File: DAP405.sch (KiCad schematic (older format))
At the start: 56 parts, among them J1 USB_B, J2 Target, J3 JTAG, U1 LT1117-3.3, U10 74LVC1G17, U11 SN74LVC1T45DBV, U12 SN74LVC1T45DBV, U13 SN74LVC1T45DBV, U14 SY6280, U2 USB3300-EZK, U3 STM32F405RGTx, U4 REF3033, U5 74LVC1G17, U6 SN74LVC1T45DBV, U7 SN74LVC1T45DBV, U8 SN74LVC1T45DBV, U9 SN74LVC1T45DBV, Y1 24M, Y2 12M

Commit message: Fixing the ULPI interface.
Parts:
- added D4: SMF5.0A, Diode_SMD:D_1206_3216Metric_Pad1.42x1.75mm_HandSolder, symbol Device:D_Zener_Small
- added F2: 200mA, Fuse:Fuse_0805_2012Metric_Pad1.15x1.40mm_HandSolder, symbol Device:Polyfuse_Small
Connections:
- net GND: now also D4.2 (A)
- net VDD: now also D4.1 (K), F2.2; no longer J2.1 (Pin_1)
- net ~RESET: no longer U2.9 (RESET)
- net ULPI_RST: now reaches U3.37 (PC6)
- net ULPI_RST: now also U2.9 (RESET)
- new net: F2.1, J2.1 (Pin_1)
- no-connect marks 22 -> 21
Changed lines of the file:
@@
 EESchema Schematic File Version 4
+LIBS:DAP405-cache
 EELAYER 29 0
 EELAYER END
@@
 ULPI_CLK
 Text Label 4000 4400 2    50   ~ 0
-~RESET
+ULPI_RST
 Wire Wire Line
 	4000 3200 3400 3200
@@
 Wire Wire Line
 	5400 6500 5400 6600
-Wire Wire Line
-	4750 6300 4100 6300
-Wire Wire Line
-	4100 6300 4100 6200
 NoConn ~ 5250 6300
 Text Label 4400 6400 0    50   ~ 0
@@
 Wire Wire Line
 	4100 6800 4750 6800
-Wire Wire Line
-	4100 6300 4100 6500
-Connection ~ 4100 6300
 Wire Wire Line
 	4100 6800 4100 6700
@@
 NoConn ~ 6900 2600
 NoConn ~ 5500 3600
-NoConn ~ 5500 3700
 NoConn ~ 5500 4100
+Text Label 5100 3700 0    50   ~ 0
+ULPI_RST
+Wire Wire Line
+	5100 3700 5500 3700
+$Comp
+L Device:D_Zener_Small D4
+U 1 1 5D90D4CC
+P 9100 4800
+F 0 "D4" V 9054 4868 50  0000 L CNN
+F 1 "SMF5.0A" V 9145 4868 50  0000 L CNN
+F 2 "Diode_SMD:D_1206_3216Metric_Pad1.42x1.75mm_HandSolder" V 9100 4800 50  0001 C CNN
+F 3 "~" V 9100 4800 50  0001 C CNN
+	1    9100 4800
+	0    1    1    0
+$EndComp
+$Comp
+L power:GND #PWR0138
+U 1 1 5D90FBB5
+P 9100 5000
+F 0 "#PWR0138" H 9100 4750 50  0001 C CNN
+F 1 "GND" H 9105 4827 50  0000 C CNN
+F 2 "" H 9100 5000 50  0001 C CNN
+F 3 "" H 9100 5000 50  0001 C CNN
+	1    9100 5000
+	1    0    0    -1
+$EndComp
+Wire Wire Line
+	9100 3700 9100 4700
+Connection ~ 9100 3700
+Wire Wire Line
+	9100 4900 9100 5000
+Wire Wire Line
+	4100 6200 4100 6300
+$Comp
+L Device:Polyfuse_Small F2
+U 1 1 5D95B670
+P 4300 6300
+F 0 "F2" V 4095 6300 50  0000 C CNN
+F 1 "200mA" V 4186 6300 50  0000 C CNN
+F 2 "Fuse:Fuse_0805_2012Metric_Pad1.15x1.40mm_HandSolder" H 4350 6100 50  0001 L CNN
+F 3 "~" H 4300 6300 50  0001 C CNN
+	1    4300 6300
+	0    1    1    0
+$EndComp
+Wire Wire Line
+	4400 6300 4750 6300
+Wire Wire Line
+	4200 6300 4100 6300
+Connection ~ 4100 6300
+Wire Wire Line
+	4100 6300 4100 6500
 $EndSCHEMATC

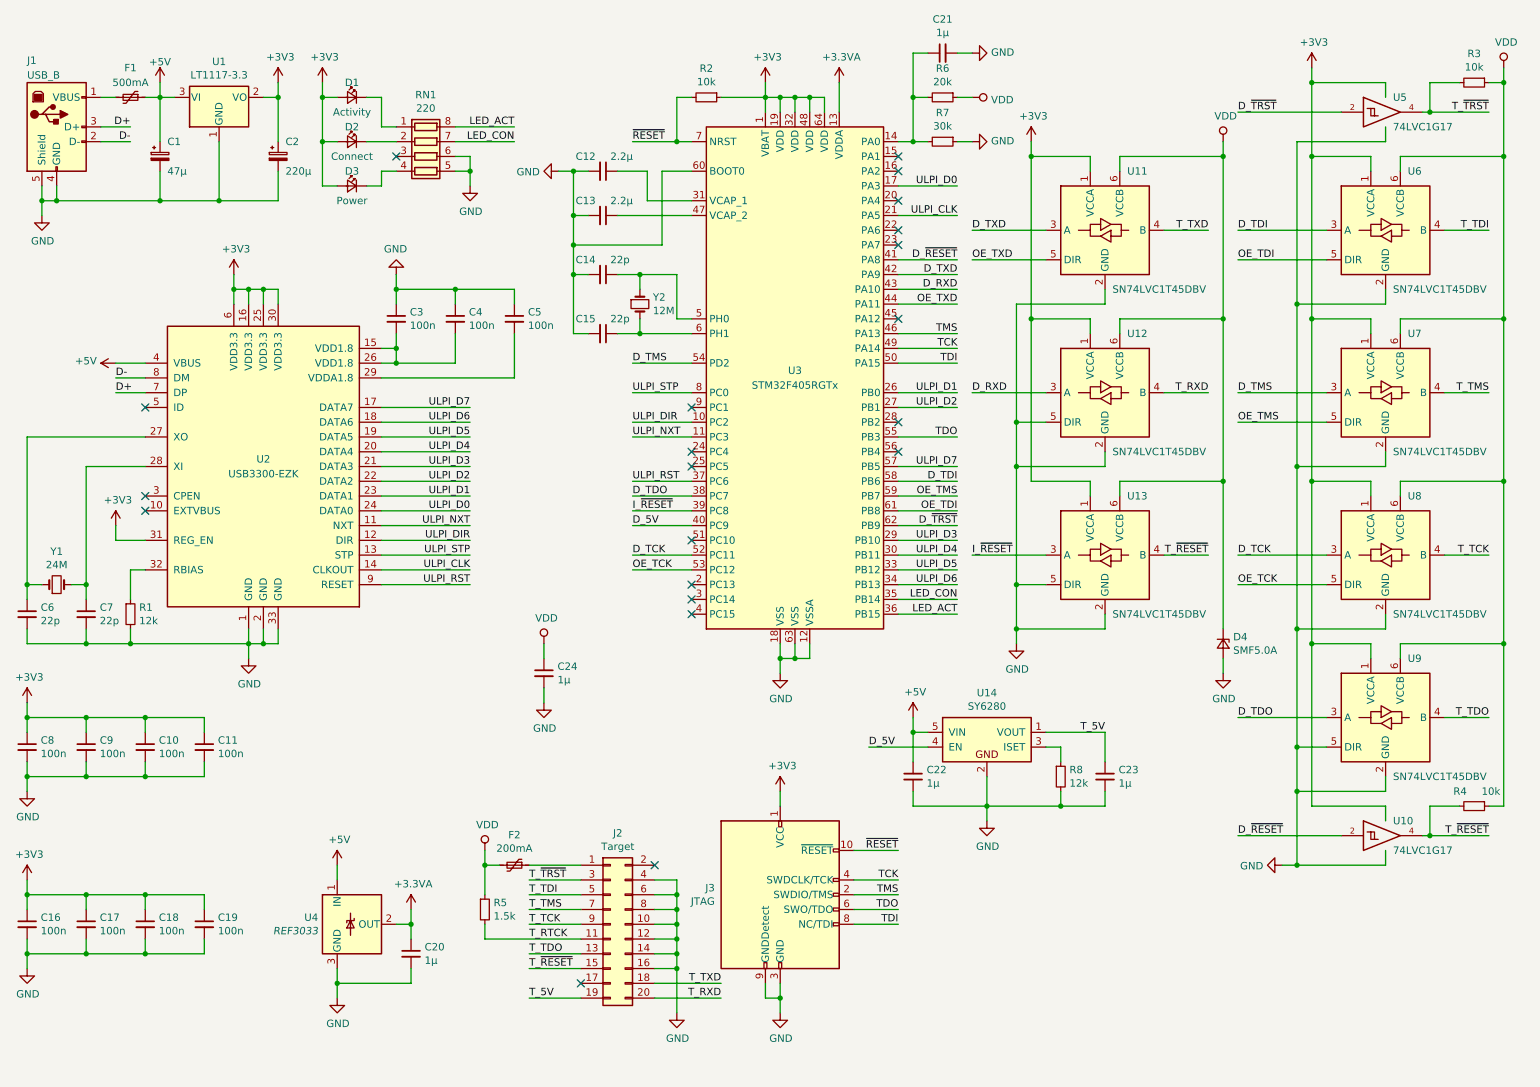
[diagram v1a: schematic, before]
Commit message: STM32F446 version
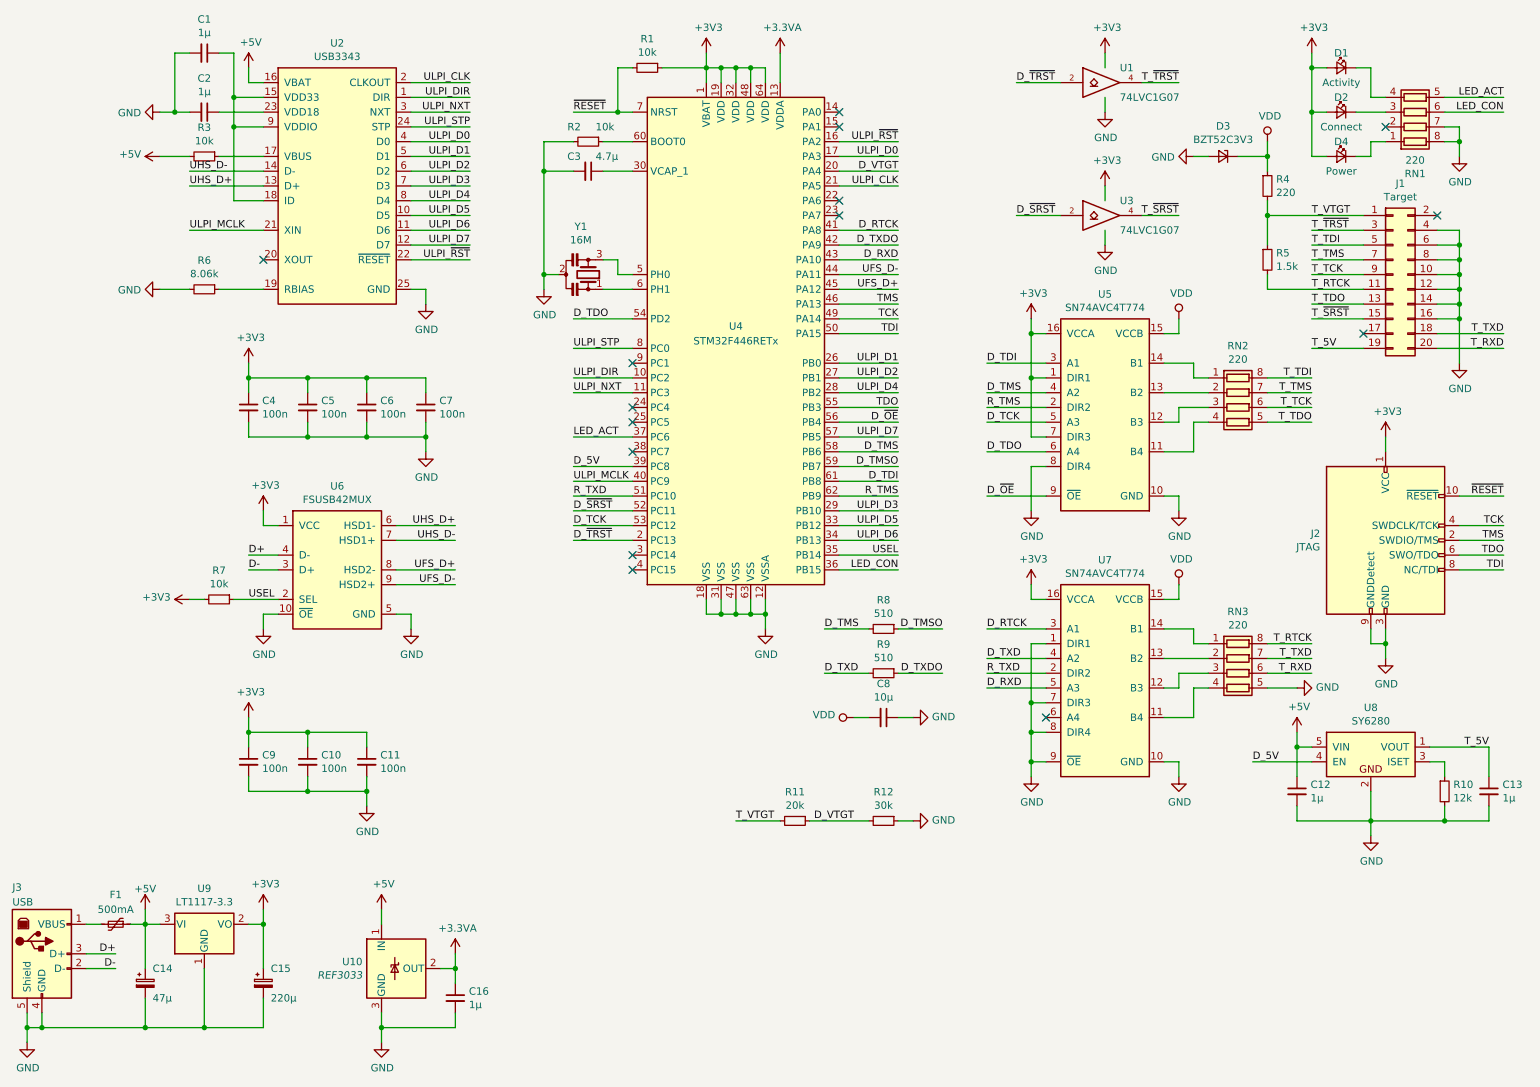
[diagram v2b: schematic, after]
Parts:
- removed C12, C13: 2.2µ, Capacitor_SMD:C_0603_1608Metric_Pad1.05x0.95mm_HandSolder, symbol Device:C_Small
- removed C14, C15: 22p, Capacitor_SMD:C_0603_1608Metric_Pad1.05x0.95mm_HandSolder, symbol Device:C_Small
- removed C16, C17, C18, C19: 100n, Capacitor_SMD:C_0603_1608Metric_Pad1.05x0.95mm_HandSolder, symbol Device:C_Small
- removed C21, C24: 1µ, Capacitor_SMD:C_0603_1608Metric_Pad1.05x0.95mm_HandSolder, symbol Device:C_Small
- removed D4: SMF5.0A, Diode_SMD:D_1206_3216Metric_Pad1.42x1.75mm_HandSolder, symbol Device:D_Zener_Small
- removed F2: 200mA, Fuse:Fuse_0805_2012Metric_Pad1.15x1.40mm_HandSolder, symbol Device:Polyfuse_Small
- removed U10, U5: 74LVC1G17, Package_TO_SOT_SMD:SOT-23-5, symbol 74xGxx:74LVC1G17
- removed U11, U12, U13, U6, U7, U8, U9: SN74LVC1T45DBV, Package_TO_SOT_SMD:SOT-23-6, symbol Logic_LevelTranslator:SN74LVC1T45DBV
- removed U2: USB3300-EZK, Package_DFN_QFN:QFN-32-1EP_5x5mm_P0.5mm_EP3.45x3.45mm, symbol Interface_USB:USB3300-EZK
- removed U3: STM32F405RGTx, Package_QFP:LQFP-64_10x10mm_P0.5mm, symbol MCU_ST_STM32F4:STM32F405RGTx
- removed Y1: 24M, Crystal:Crystal_SMD_5032-2Pin_5.0x3.2mm, symbol Device:Crystal_Small
- removed Y2: 12M, Crystal:Crystal_SMD_5032-2Pin_5.0x3.2mm, symbol Device:Crystal_Small
- added C1, C2: 1µ, Capacitor_SMD:C_0603_1608Metric_Pad1.05x0.95mm_HandSolder, symbol Device:C_Small
- added D3: BZT52C3V3, Diode_SMD:D_SOD-123, symbol Device:D_Zener_Small
- added R11: 20k, Resistor_SMD:R_0603_1608Metric_Pad1.05x0.95mm_HandSolder, symbol Device:R_Small
- added R12: 30k, Resistor_SMD:R_0603_1608Metric_Pad1.05x0.95mm_HandSolder, symbol Device:R_Small
- added R8, R9: 510, Resistor_SMD:R_0603_1608Metric_Pad1.05x0.95mm_HandSolder, symbol Device:R_Small
- added RN2, RN3: 220, Resistor_SMD:R_Array_Convex_4x0603, symbol Device:R_Pack04
- added U1, U3: 74LVC1G07, Package_TO_SOT_SMD:SOT-23-5, symbol 74xGxx:74LVC1G07
- added U2: USB3343, Package_DFN_QFN:QFN-24-1EP_4x4mm_P0.5mm_EP2.6x2.6mm, symbol Interface_USB:USB3343
- added U4: STM32F446RETx, Package_QFP:LQFP-64_10x10mm_P0.5mm, symbol MCU_ST_STM32F4:STM32F446RETx
- added U5, U7: SN74AVC4T774, Package_SO:TSSOP-16_4.4x5mm_P0.65mm, symbol Logic_LevelTranslator:SN74AVC4T774
- added U6: FSUSB42MUX, Package_SO:MSOP-10_3x3mm_P0.5mm, symbol Analog_Switch:FSUSB42MUX
- added Y1: 16M, Crystal:Resonator_SMD_muRata_CSTxExxV-3Pin_3.0x1.1mm, symbol Device:Resonator_Small
- C3: value 100n -> 4.7µ
- C6, C7: value 22p -> 100n
- C8: value 100n -> 10µ; footprint Capacitor_SMD:C_0603_1608Metric_Pad1.05x0.95mm_HandSolder -> Capacitor_SMD:C_0805_2012Metric_Pad1.15x1.40mm_HandSolder
- J3: renamed from J1; value USB_B -> USB
- R1: value 12k -> 10k
- R4: value 10k -> 220
- R6: value 20k -> 8.06k
- R7: value 30k -> 10k
- renumbered C22 to C12, C23 to C13, C1 to C14, C2 to C15, C20 to C16, D3 to D4, J2 to J1, J3 to J2, R8 to R10, U4 to U10, U14 to U8, U1 to U9
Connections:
- net +3.3VA: now also U4.13 (VDDA)
- net +3V3: now also C4.1, C5.1, C6.1, C7.1, R1.1, R7.2, U1.5 (VCC), U3.5 (VCC), U4.1 (VBAT), U4.19 (VDD), U4.32 (VDD), U4.48 (VDD), U4.64 (VDD), U5.1 (DIR1), U5.16 (VCCA), U5.7 (DIR3), U6.1 (VCC), U7.16 (VCCA); no longer C8.1, R2.1
- net +5V: now also R3.2, U2.16 (VBAT)
- net D+: now also U6.4 (D-)
- net D-: now also U6.3 (D+)
- net D_5V: now also U4.39 (PC8)
- net D_RXD: now also U4.43 (PA10), U7.5 (A3)
- net D_TCK: now also U4.53 (PC12), U5.5 (A3)
- net D_TDI: now also U4.61 (PB8), U5.3 (A1)
- net D_TDO: now also U4.54 (PD2), U5.6 (A4)
- net D_TMS: now also R8.2, U4.58 (PB6), U5.4 (A2)
- net D_TXD: now also R9.2, U7.4 (A2)
- net D_~TRST: now also U1.2, U4.2 (PC13)
- net GND: now also C3.2, C4.2, C5.2, C8.1, R2.2, R6.2, RN1.7 (R2.2), RN1.8 (R1.2), C1.2, C2.2, D3.2 (A), R12.1, RN3.5 (R4.2), U1.3 (GND), U2.25 (GND), U3.3 (GND), U4.12 (VSSA), U4.18 (VSS), U4.31 (VSS), U4.47 (VSS), U4.63 (VSS), U5.10 (GND), U5.8 (DIR4), U6.10 (~OE), U6.5 (GND), U7.1 (DIR1), U7.10 (GND), U7.7 (DIR3), U7.8 (DIR4), U7.9 (~OE), Y1.2; no longer C3.1, C4.1, C5.1, C8.2, R1.2, R7.1, RN1.5 (R4.2), RN1.6 (R3.2)
- net LED_ACT: now also RN1.5 (R4.2), U4.37 (PC6); no longer RN1.8 (R1.2)
- net LED_CON: now also RN1.6 (R3.2), U4.36 (PB15); no longer RN1.7 (R2.2)
- net TCK: now also U4.49 (PA14)
- net TDI: now also U4.50 (PA15)
- net TDO: now also U4.55 (PB3)
- net TMS: now also U4.46 (PA13)
- net T_RTCK: now also RN3.8 (R1.2)
- net T_RXD: now also RN3.6 (R3.2)
- net T_TCK: now also RN2.6 (R3.2)
- net T_TDI: now also RN2.8 (R1.2)
- net T_TDO: now also RN2.5 (R4.2)
- net T_TMS: now also RN2.7 (R2.2)
- net T_TXD: now also RN3.7 (R2.2)
- net T_~TRST: now also U1.4; no longer R3.2
- net ULPI_CLK: now also U2.2 (CLKOUT), U4.21 (PA5)
- net ULPI_D0: now also U2.4 (D0), U4.17 (PA3)
- net ULPI_D1: now also U2.5 (D1), U4.26 (PB0)
- net ULPI_D2: now also U2.6 (D2), U4.27 (PB1)
- net ULPI_D3: now also U2.7 (D3), U4.29 (PB10)
- net ULPI_D4: now also U2.8 (D4), U4.28 (PB2)
- net ULPI_D5: now also U2.10 (D5), U4.33 (PB12)
- net ULPI_D6: now also U2.11 (D6), U4.34 (PB13)
- net ULPI_D7: now also U2.12 (D7), U4.57 (PB5)
- net ULPI_DIR: now also U2.1 (DIR), U4.10 (PC2)
- net ULPI_NXT: now also U2.3 (NXT), U4.11 (PC3)
- net ULPI_STP: now also U2.24 (STP), U4.8 (PC0)
- net VDD: now also C8.2, D3.1 (K), U5.15 (VCCB), U7.15 (VCCB); no longer R3.1, R5.1, R6.1
- net ~RESET: now also R1.2, U4.7 (NRST); no longer R2.2
- net at D2.1 (K): now also RN1.3 (R3.1); no longer RN1.2 (R2.1)
- net at D1.1 (K): now also RN1.4 (R4.1); no longer RN1.1 (R1.1)
- net at D4.1 (K): now also RN1.1 (R1.1); no longer RN1.4 (R4.1)
- net T_VTGT: now reaches J1.1 (Pin_1)
- net T_VTGT: now also R4.2, R5.1, R11.2
- net T_~RESET renamed T_~SRST
- net T_~SRST: now also U3.4; no longer R4.2
- new net: RN2.4 (R4.1), U5.11 (B4)
- new net: RN2.3 (R3.1), U5.12 (B3)
- new net: RN2.2 (R2.1), U5.13 (B2)
- new net: RN2.1 (R1.1), U5.14 (B1)
- new net: RN3.4 (R4.1), U7.11 (B4)
- new net: RN3.3 (R3.1), U7.12 (B3)
- new net: RN3.2 (R2.1), U7.13 (B2)
- new net: RN3.1 (R1.1), U7.14 (B1)
- new net: C3.1, U4.30 (VCAP_1)
- new net: U4.5 (PH0), Y1.3
- new net: U4.6 (PH1), Y1.1
- new net: R2.1, U4.60 (BOOT0)
- new net: C1.1, U2.15 (VDD33), U2.18 (ID), U2.9 (VDDIO)
- new net: R3.1, U2.17 (VBUS)
- new net: R6.1, U2.19 (RBIAS)
- new net: C2.1, U2.23 (VDD18)
- new net D_RTCK: U4.41 (PA8), U7.3 (A1)
- new net D_TMSO: R8.1, U4.59 (PB7)
- new net D_TXDO: R9.1, U4.42 (PA9)
- new net D_VTGT: R11.1, R12.2, U4.20 (PA4)
- new net D_~OE: U4.56 (PB4), U5.9 (~OE)
- new net D_~SRST: U3.2, U4.52 (PC11)
- new net R_TMS: U4.62 (PB9), U5.2 (DIR2)
- new net R_TXD: U4.51 (PC10), U7.2 (DIR2)
- new net UFS_D+: U4.45 (PA12), U6.8 (HSD2-)
- new net UFS_D-: U4.44 (PA11), U6.9 (HSD2+)
- new net UHS_D+: U2.13 (D+), U6.6 (HSD1-)
- new net UHS_D-: U2.14 (D-), U6.7 (HSD1+)
- new net ULPI_MCLK: U2.21 (XIN), U4.40 (PC9)
- new net ULPI_~RST: U2.22 (~RESET), U4.16 (PA2)
- new net USEL: R7.1, U4.35 (PB14), U6.2 (SEL)
- no-connect marks 21 -> 15
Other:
- moved on the sheet: C12, C13, C14, C15, C16, D1, D2, D4, F1, J1, J2, J3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
